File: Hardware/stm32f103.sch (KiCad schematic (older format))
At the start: 9 parts, among them U2 STM32F102C8Tx

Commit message: Replaced gate driver with opamp. Replaced feedback circuit with unity gain buffer
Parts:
- added D1: LED_Small_ALT, Capacitor_SMD:C_0805_2012Metric_Pad1.15x1.40mm_HandSolder, symbol Device:LED_Small_ALT
- added R3: 1k, Resistor_SMD:R_0603_1608Metric_Pad1.05x0.95mm_HandSolder, symbol Device:R_Small
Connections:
- wire segments 43 -> 46
- no-connect marks 28 -> 27
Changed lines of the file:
@@
 ADC
 Wire Wire Line
-	5800 4800 5900 4800
-Wire Wire Line
 	5900 1800 6000 1800
-$Comp
-L MCU_ST_STM32F1:STM32F102C8Tx U2
-U 1 1 5F7B3DDF
-P 5900 3300
-F 0 "U2" H 6200 1800 50  0000 C CNN
-F 1 "STM32F102C8Tx" H 6450 1700 50  0000 C CNN
-F 2 "Package_QFP:LQFP-48_7x7mm_P0.5mm" H 5300 1900 50  0001 R CNN
-F 3 "http://www.st.com/st-web-ui/static/active/en/resource/technical/document/datasheet/CD00210831.pdf" H 5900 3300 50  0001 C CNN
-	1    5900 3300
-	1    0    0    -1
-$EndComp
 Wire Wire Line
 	6250 1600 6250 1800
 Wire Wire Line
 	6250 1800 6100 1800
-Wire Wire Line
-	6000 4800 5900 4800
-Connection ~ 5900 4800
 Text HLabel 4850 3600 0    50   Input ~ 0
 OLED_RST
@@
 NoConn ~ 5200 4400
 NoConn ~ 5200 4500
-NoConn ~ 5200 4600
 NoConn ~ 6500 4600
 NoConn ~ 6500 4300
@@
 Text Notes 6850 4000 0    50   ~ 0
 Needs to run at >500kHz
+Wire Wire Line
+	6000 4800 5900 4800
+Wire Wire Line
+	5800 4800 5900 4800
+Connection ~ 5900 4800
+$Comp
+L MCU_ST_STM32F1:STM32F102C8Tx U2
+U 1 1 5F7B3DDF
+P 5900 3300
+F 0 "U2" H 6200 1800 50  0000 C CNN
+F 1 "STM32F102C8Tx" H 6450 1700 50  0000 C CNN
+F 2 "Package_QFP:LQFP-48_7x7mm_P0.5mm" H 5300 1900 50  0001 R CNN
+F 3 "http://www.st.com/st-web-ui/static/active/en/resource/technical/document/datasheet/CD00210831.pdf" H 5900 3300 50  0001 C CNN
+	1    5900 3300
+	1    0    0    -1
+$EndComp
+$Comp
+L Device:LED_Small_ALT D?
+U 1 1 5F81F246
+P 5050 5100
+AR Path="/5F7C24CB/5F81F246" Ref="D?"  Part="1"
+AR Path="/5F7B3BD2/5F81F246" Ref="D1"  Part="1"
+F 0 "D1" V 5096 5030 50  0000 R CNN
+F 1 "LED_Small_ALT" V 5005 5030 50  0000 R CNN
+F 2 "Capacitor_SMD:C_0805_2012Metric_Pad1.15x1.40mm_HandSolder" V 5050 5100 50  0001 C CNN
+F 3 "~" V 5050 5100 50  0001 C CNN
+	1    5050 5100
+	0    -1   -1   0
+$EndComp
+$Comp
+L power:GND #PWR?
+U 1 1 5F81F24D
+P 5050 5200
+AR Path="/5F7C24CB/5F81F24D" Ref="#PWR?"  Part="1"
+AR Path="/5F7B3BD2/5F81F24D" Ref="#PWR0109"  Part="1"
+F 0 "#PWR0109" H 5050 4950 50  0001 C CNN
+F 1 "GND" H 5055 5027 50  0000 C CNN
+F 2 "" H 5050 5200 50  0001 C CNN
+F 3 "" H 5050 5200 50  0001 C CNN
+	1    5050 5200
+	1    0    0    -1
+$EndComp
+$Comp
+L Device:R_Small R3
+U 1 1 5F820741
+P 5050 4775
+F 0 "R3" V 4854 4775 50  0000 C CNN
+F 1 "1k" V 4945 4775 50  0000 C CNN
+F 2 "Resistor_SMD:R_0603_1608Metric_Pad1.05x0.95mm_HandSolder" H 5050 4775 50  0001 C CNN
+F 3 "~" H 5050 4775 50  0001 C CNN
+	1    5050 4775
+	-1   0    0    1
+$EndComp
+Wire Wire Line
+	5050 4675 5050 4600
+Wire Wire Line
+	5050 4600 5200 4600
+Wire Wire Line
+	5050 4875 5050 5000
 $EndSCHEMATC

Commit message: Changed the PWM control circuit
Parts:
- removed U2: STM32F102C8Tx, Package_QFP:LQFP-48_7x7mm_P0.5mm, symbol MCU_ST_STM32F1:STM32F102C8Tx
- added U2: STM32F103C8Tx, Package_QFP:LQFP-48_7x7mm_P0.5mm, symbol MCU_ST_STM32F1:STM32F103C8Tx
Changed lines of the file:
@@
 Text Notes 6850 4000 0    50   ~ 0
 Needs to run at >500kHz
-Wire Wire Line
-	6000 4800 5900 4800
-Wire Wire Line
-	5800 4800 5900 4800
-Connection ~ 5900 4800
-$Comp
-L MCU_ST_STM32F1:STM32F102C8Tx U2
-U 1 1 5F7B3DDF
-P 5900 3300
-F 0 "U2" H 6200 1800 50  0000 C CNN
-F 1 "STM32F102C8Tx" H 6450 1700 50  0000 C CNN
-F 2 "Package_QFP:LQFP-48_7x7mm_P0.5mm" H 5300 1900 50  0001 R CNN
-F 3 "http://www.st.com/st-web-ui/static/active/en/resource/technical/document/datasheet/CD00210831.pdf" H 5900 3300 50  0001 C CNN
-	1    5900 3300
-	1    0    0    -1
-$EndComp
 $Comp
 L Device:LED_Small_ALT D?
@@
 Wire Wire Line
 	5050 4875 5050 5000
+$Comp
+L MCU_ST_STM32F1:STM32F103C8Tx U2
+U 1 1 5F8CF7B9
+P 5900 3300
+F 0 "U2" H 6275 1800 50  0000 C CNN
+F 1 "STM32F103C8Tx" H 6525 1650 50  0000 C CNN
+F 2 "Package_QFP:LQFP-48_7x7mm_P0.5mm" H 5300 1900 50  0001 R CNN
+F 3 "http://www.st.com/st-web-ui/static/active/en/resource/technical/document/datasheet/CD00161566.pdf" H 5900 3300 50  0001 C CNN
+	1    5900 3300
+	1    0    0    -1
+$EndComp
+Wire Wire Line
+	5900 4800 6000 4800
+Wire Wire Line
+	5800 4800 5900 4800
+Connection ~ 5900 4800
 $EndSCHEMATC

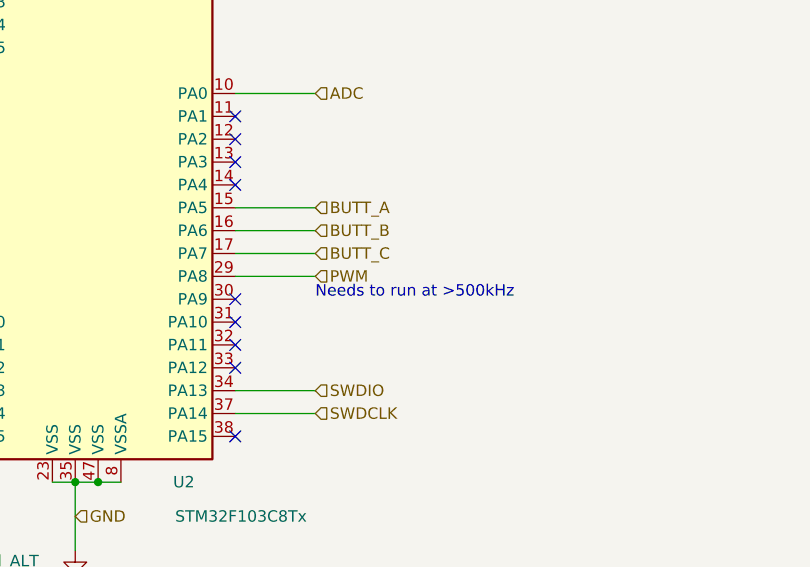
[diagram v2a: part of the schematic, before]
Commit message: Added ADC instead of opamp. Added stiching
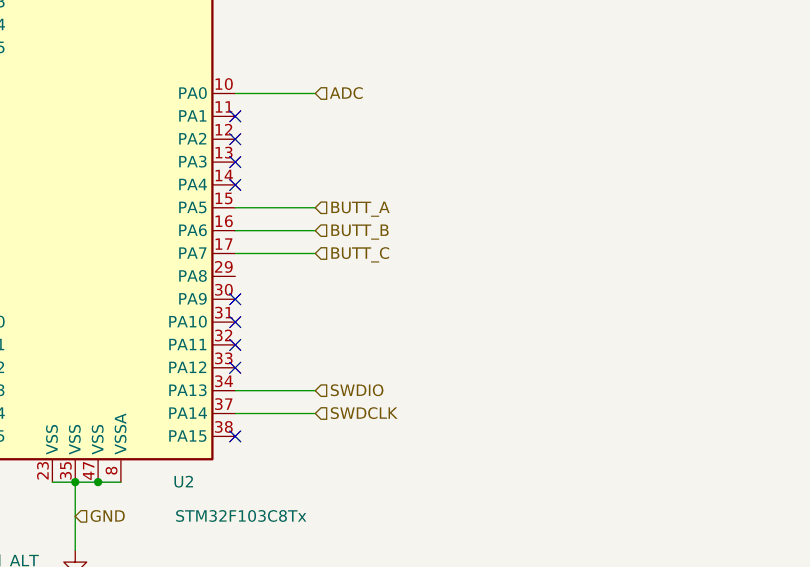
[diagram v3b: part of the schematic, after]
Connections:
- net PWM: no longer names the net of U2.29 (PA8)
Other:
- note removed: "Needs to run at >500kHz"
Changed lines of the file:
@@
 Wire Wire Line
 	10200 1850 10400 1850
-Wire Wire Line
-	6500 3900 6850 3900
-Text HLabel 6850 3900 2    50   Input ~ 0
-PWM
 NoConn ~ 5200 2400
 NoConn ~ 5200 2500
@@
 	4850 3600 5200 3600
 NoConn ~ 6500 3500
-Text Notes 6850 4000 0    50   ~ 0
-Needs to run at >500kHz
 $Comp
 L Device:LED_Small_ALT D?

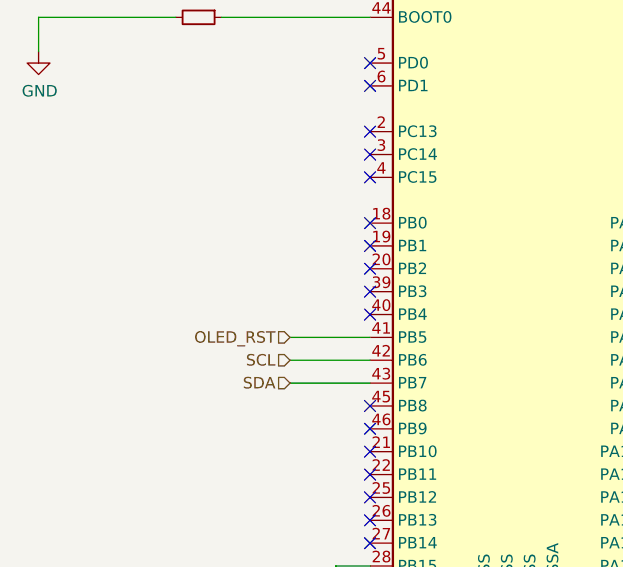
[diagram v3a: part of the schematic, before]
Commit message: Added pull up resistors on I2C line, added BOM
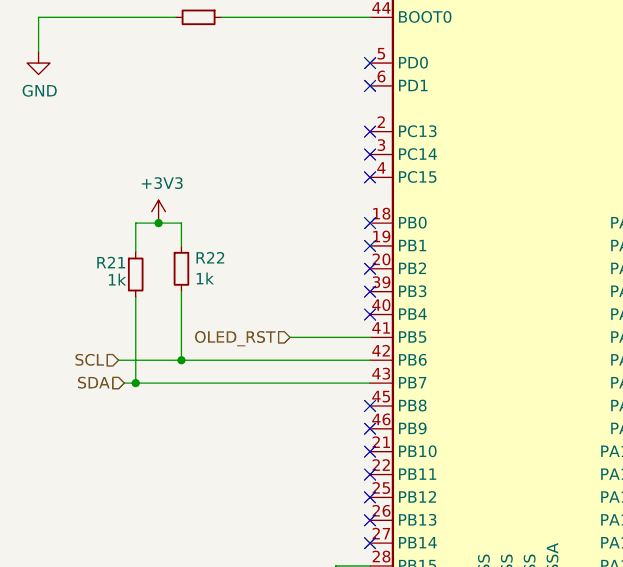
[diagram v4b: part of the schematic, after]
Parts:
- added R21, R22: 1k, Resistor_SMD:R_0603_1608Metric_Pad1.05x0.95mm_HandSolder, symbol Device:R_Small
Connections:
- net +3V3: now also R21.1, R22.1
- net SCL: now also R22.2
- net SDA: now also R21.2
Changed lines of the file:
@@
 Comment4 ""
 $EndDescr
-$Comp
-L power:+3V3 #PWR0117
-U 1 1 5F7B523E
-P 5900 1600
-F 0 "#PWR0117" H 5900 1450 50  0001 C CNN
-F 1 "+3V3" H 5915 1773 50  0000 C CNN
-F 2 "" H 5900 1600 50  0001 C CNN
-F 3 "" H 5900 1600 50  0001 C CNN
-	1    5900 1600
-	1    0    0    -1
-$EndComp
 Wire Wire Line
 	5800 1800 5900 1800
@@
 Wire Wire Line
 	5800 4800 5800 5100
-Wire Wire Line
-	6500 4400 6850 4400
-Wire Wire Line
-	6500 4500 6850 4500
 Text HLabel 5050 2000 0    50   Input ~ 0
 ~RST
@@
 Text HLabel 5800 4950 2    50   Input ~ 0
 GND
-Wire Wire Line
-	5200 3700 4850 3700
-Wire Wire Line
-	5200 3800 4850 3800
-Text HLabel 4850 3700 0    50   Input ~ 0
+Text HLabel 4100 3700 0    50   Input ~ 0
 SCL
-Text HLabel 4850 3800 0    50   Input ~ 0
+Text HLabel 4125 3800 0    50   Input ~ 0
 SDA
 Wire Wire Line
@@
 	5800 4800 5900 4800
 Connection ~ 5900 4800
+$Comp
+L Device:R_Small R21
+U 1 1 5F7FD574
+P 4175 3325
+F 0 "R21" H 4000 3375 50  0000 L CNN
+F 1 "1k" H 4050 3300 50  0000 L CNN
+F 2 "Resistor_SMD:R_0603_1608Metric_Pad1.05x0.95mm_HandSolder" H 4175 3325 50  0001 C CNN
+F 3 "~" H 4175 3325 50  0001 C CNN
+	1    4175 3325
+	1    0    0    -1
+$EndComp
+$Comp
+L Device:R_Small R22
+U 1 1 5F7FE183
+P 4375 3300
+F 0 "R22" H 4434 3346 50  0000 L CNN
+F 1 "1k" H 4434 3255 50  0000 L CNN
+F 2 "Resistor_SMD:R_0603_1608Metric_Pad1.05x0.95mm_HandSolder" H 4375 3300 50  0001 C CNN
+F 3 "~" H 4375 3300 50  0001 C CNN
+	1    4375 3300
+	1    0    0    -1
+$EndComp
+Wire Wire Line
+	4175 3425 4175 3800
+Wire Wire Line
+	4375 3400 4375 3700
+$Comp
+L power:+3V3 #PWR0117
+U 1 1 5F7B523E
+P 5900 1600
+F 0 "#PWR0117" H 5900 1450 50  0001 C CNN
+F 1 "+3V3" H 5915 1773 50  0000 C CNN
+F 2 "" H 5900 1600 50  0001 C CNN
+F 3 "" H 5900 1600 50  0001 C CNN
+	1    5900 1600
+	1    0    0    -1
+$EndComp
+$Comp
+L power:+3V3 #PWR02
+U 1 1 5F800EB2
+P 4275 3100
+F 0 "#PWR02" H 4275 2950 50  0001 C CNN
+F 1 "+3V3" H 4290 3273 50  0000 C CNN
+F 2 "" H 4275 3100 50  0001 C CNN
+F 3 "" H 4275 3100 50  0001 C CNN
+	1    4275 3100
+	1    0    0    -1
+$EndComp
+Wire Wire Line
+	4275 3100 4175 3100
+Wire Wire Line
+	4175 3100 4175 3225
+Wire Wire Line
+	4275 3100 4375 3100
+Wire Wire Line
+	4375 3100 4375 3200
+Connection ~ 4275 3100
+Wire Wire Line
+	6500 4400 6850 4400
+Wire Wire Line
+	6500 4500 6850 4500
+Connection ~ 4175 3800
+Wire Wire Line
+	4175 3800 4125 3800
+Connection ~ 4375 3700
+Wire Wire Line
+	4375 3700 4100 3700
+Wire Wire Line
+	4375 3700 5200 3700
+Wire Wire Line
+	4175 3800 5200 3800
 $EndSCHEMATC

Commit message: updated C1 footprint, updated MCU schematic. Fixed possible issue with buttons
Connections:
- net +3V3: now also U2.1 (VBAT)
- no-connect marks 27 -> 26
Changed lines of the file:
@@
 encoding utf-8
 Sheet 2 4
-Title ""
-Date ""
-Rev ""
+Title "Electronic Load"
+Date "2020-10-12"
+Rev "0.0.1"
 Comp ""
 Comment1 ""
@@
 $EndComp
 Wire Wire Line
-	5500 1700 5900 1700
+	5500 1700 5700 1700
 Wire Wire Line
 	5900 1600 5900 1700
@@
 NoConn ~ 6500 3300
 NoConn ~ 6500 3200
-NoConn ~ 5700 1800
 $Comp
 L power:VDDA #PWR0122
@@
 Wire Wire Line
 	4175 3800 5200 3800
+Wire Wire Line
+	5700 1800 5700 1700
+Connection ~ 5700 1700
+Wire Wire Line
+	5700 1700 5900 1700
 $EndSCHEMATC
